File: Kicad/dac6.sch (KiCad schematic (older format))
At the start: 13 parts

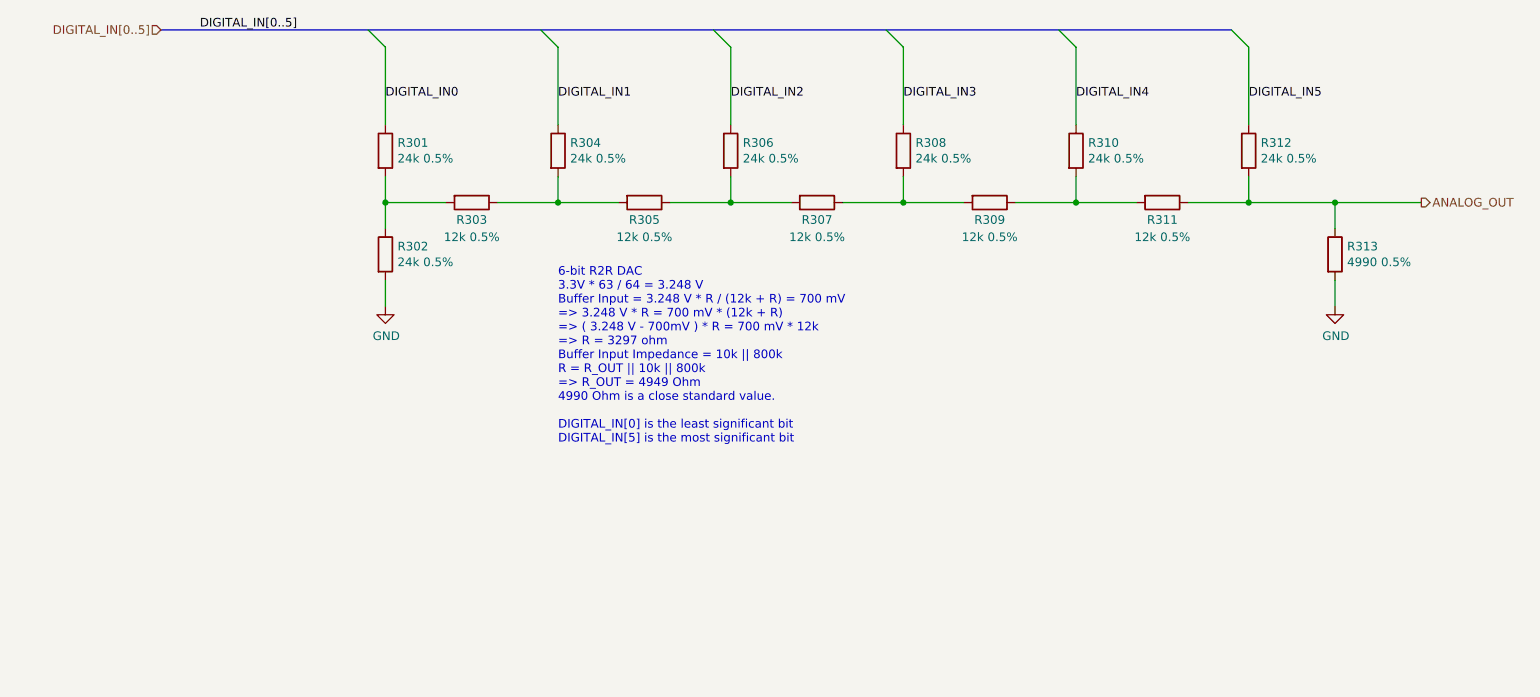
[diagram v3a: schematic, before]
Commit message: Changes to BMC
* Swapped BUTTON_PWR and SYS_RESET to avoid DRC issue
* Split PSU and BMC into two separate sheets
* Swapped some pins on the STM32 to make it compatible with more
alternatives
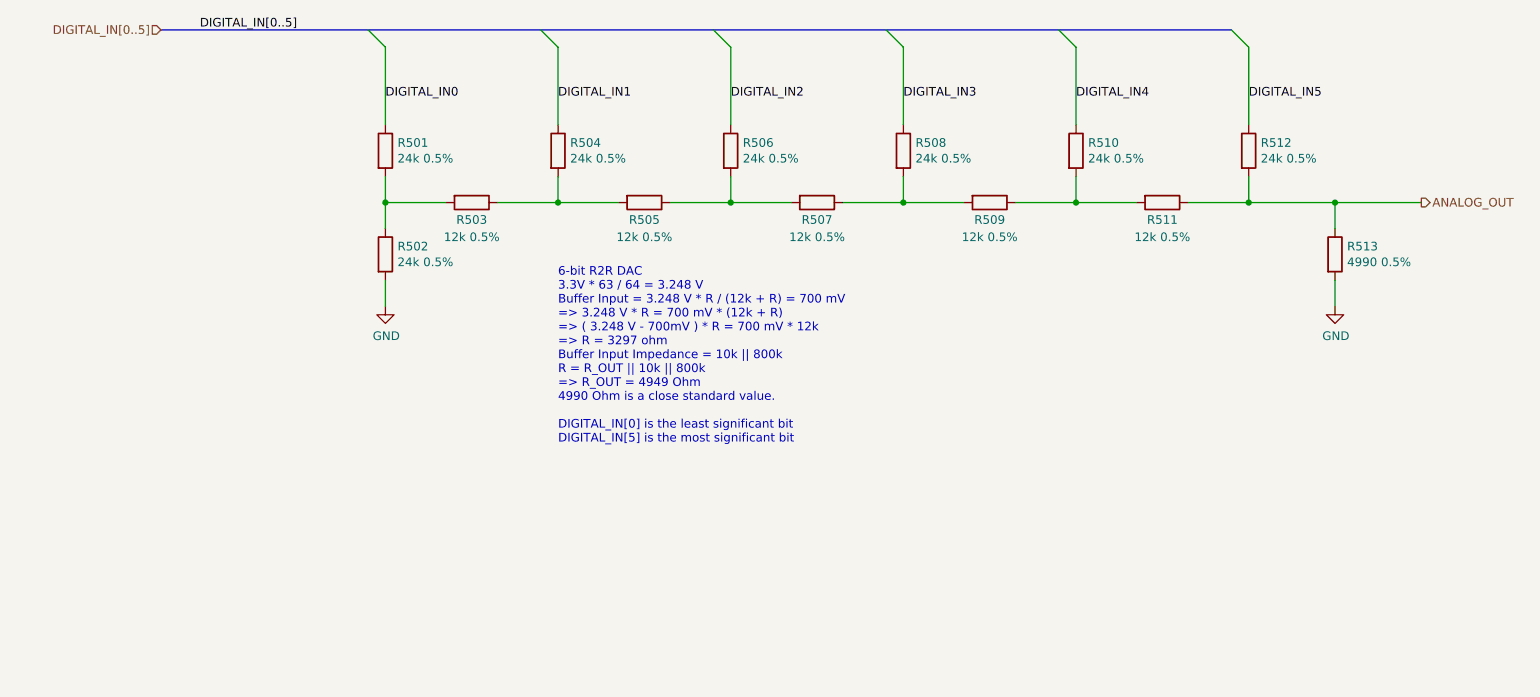
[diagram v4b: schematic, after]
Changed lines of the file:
@@
 $Descr A4 11693 8268
 encoding utf-8
-Sheet 3 16
+Sheet 3 17
 Title "Neotron Common Hardware - 6-bit DAC"
 Date "2021-04-02"
@@
 AR Path="/5FDE658D/60682025/60681FF8" Ref="R301"  Part="1"
 AR Path="/5FDE658D/6068202F/60681FF8" Ref="R501"  Part="1"
-F 0 "R301" H 3570 2746 50  0000 L CNN
+F 0 "R501" H 3570 2746 50  0000 L CNN
 F 1 "24k 0.5%" H 3570 2655 50  0000 L CNN
 F 2 "Resistor_SMD:R_0805_2012Metric_Pad1.20x1.40mm_HandSolder" V 3430 2700 50  0001 C CNN
@@
 AR Path="/5FDE658D/60682025/5F5F5C61" Ref="R303"  Part="1"
 AR Path="/5FDE658D/6068202F/5F5F5C61" Ref="R503"  Part="1"
-F 0 "R303" V 4100 3000 50  0000 C CNN
+F 0 "R503" V 4100 3000 50  0000 C CNN
 F 1 "12k 0.5%" V 4200 3000 50  0000 C CNN
 F 2 "Resistor_SMD:R_0805_2012Metric_Pad1.20x1.40mm_HandSolder" V 3930 3000 50  0001 C CNN
@@
 AR Path="/5FDE658D/60682025/5F5F6568" Ref="R304"  Part="1"
 AR Path="/5FDE658D/6068202F/5F5F6568" Ref="R504"  Part="1"
-F 0 "R304" H 4570 2746 50  0000 L CNN
+F 0 "R504" H 4570 2746 50  0000 L CNN
 F 1 "24k 0.5%" H 4570 2655 50  0000 L CNN
 F 2 "Resistor_SMD:R_0805_2012Metric_Pad1.20x1.40mm_HandSolder" V 4430 2700 50  0001 C CNN
@@
 AR Path="/5FDE658D/60682025/5F5F6D42" Ref="R305"  Part="1"
 AR Path="/5FDE658D/6068202F/5F5F6D42" Ref="R505"  Part="1"
-F 0 "R305" V 5100 3000 50  0000 C CNN
+F 0 "R505" V 5100 3000 50  0000 C CNN
 F 1 "12k 0.5%" V 5200 3000 50  0000 C CNN
 F 2 "Resistor_SMD:R_0805_2012Metric_Pad1.20x1.40mm_HandSolder" V 4930 3000 50  0001 C CNN
@@
 AR Path="/5FDE658D/60682025/5F5F6F45" Ref="R307"  Part="1"
 AR Path="/5FDE658D/6068202F/5F5F6F45" Ref="R507"  Part="1"
-F 0 "R307" V 6100 3000 50  0000 C CNN
+F 0 "R507" V 6100 3000 50  0000 C CNN
 F 1 "12k 0.5%" V 6200 3000 50  0000 C CNN
 F 2 "Resistor_SMD:R_0805_2012Metric_Pad1.20x1.40mm_HandSolder" V 5930 3000 50  0001 C CNN
@@
 AR Path="/5FDE658D/60682025/5F5F984D" Ref="R309"  Part="1"
 AR Path="/5FDE658D/6068202F/5F5F984D" Ref="R509"  Part="1"
-F 0 "R309" V 7100 3000 50  0000 C CNN
+F 0 "R509" V 7100 3000 50  0000 C CNN
 F 1 "12k 0.5%" V 7200 3000 50  0000 C CNN
 F 2 "Resistor_SMD:R_0805_2012Metric_Pad1.20x1.40mm_HandSolder" V 6930 3000 50  0001 C CNN
@@
 AR Path="/5FDE658D/60682025/5F5F99D6" Ref="R311"  Part="1"
 AR Path="/5FDE658D/6068202F/5F5F99D6" Ref="R511"  Part="1"
-F 0 "R311" V 8100 3000 50  0000 C CNN
+F 0 "R511" V 8100 3000 50  0000 C CNN
 F 1 "12k 0.5%" V 8200 3000 50  0000 C CNN
 F 2 "Resistor_SMD:R_0805_2012Metric_Pad1.20x1.40mm_HandSolder" V 7930 3000 50  0001 C CNN
@@
 AR Path="/5FDE658D/60682025/5F5FA2EE" Ref="R313"  Part="1"
 AR Path="/5FDE658D/6068202F/5F5FA2EE" Ref="R513"  Part="1"
-F 0 "R313" H 9070 3346 50  0000 L CNN
+F 0 "R513" H 9070 3346 50  0000 L CNN
 F 1 "4990 0.5%" H 9070 3255 50  0000 L CNN
 F 2 "Resistor_SMD:R_0805_2012Metric_Pad1.20x1.40mm_HandSolder" V 8930 3300 50  0001 C CNN
@@
 AR Path="/5FDE658D/60682025/5F5FBB89" Ref="#PWR0301"  Part="1"
 AR Path="/5FDE658D/6068202F/5F5FBB89" Ref="#PWR0501"  Part="1"
-F 0 "#PWR0301" H 3500 3350 50  0001 C CNN
+F 0 "#PWR0501" H 3500 3350 50  0001 C CNN
 F 1 "GND" H 3505 3427 50  0000 C CNN
 F 2 "" H 3500 3600 50  0001 C CNN
@@
 AR Path="/5FDE658D/60682025/5F5FBF42" Ref="#PWR0302"  Part="1"
 AR Path="/5FDE658D/6068202F/5F5FBF42" Ref="#PWR0502"  Part="1"
-F 0 "#PWR0302" H 9000 3350 50  0001 C CNN
+F 0 "#PWR0502" H 9000 3350 50  0001 C CNN
 F 1 "GND" H 9005 3427 50  0000 C CNN
 F 2 "" H 9000 3600 50  0001 C CNN
@@
 AR Path="/5FDE658D/60682025/5F5FCF8C" Ref="R302"  Part="1"
 AR Path="/5FDE658D/6068202F/5F5FCF8C" Ref="R502"  Part="1"
-F 0 "R302" H 3570 3346 50  0000 L CNN
+F 0 "R502" H 3570 3346 50  0000 L CNN
 F 1 "24k 0.5%" H 3570 3255 50  0000 L CNN
 F 2 "Resistor_SMD:R_0805_2012Metric_Pad1.20x1.40mm_HandSolder" V 3430 3300 50  0001 C CNN
@@
 AR Path="/5FDE658D/60682025/5F5FD13B" Ref="R306"  Part="1"
 AR Path="/5FDE658D/6068202F/5F5FD13B" Ref="R506"  Part="1"
-F 0 "R306" H 5570 2746 50  0000 L CNN
+F 0 "R506" H 5570 2746 50  0000 L CNN
 F 1 "24k 0.5%" H 5570 2655 50  0000 L CNN
 F 2 "Resistor_SMD:R_0805_2012Metric_Pad1.20x1.40mm_HandSolder" V 5430 2700 50  0001 C CNN
@@
 AR Path="/5FDE658D/60682025/60682004" Ref="R308"  Part="1"
 AR Path="/5FDE658D/6068202F/60682004" Ref="R508"  Part="1"
-F 0 "R308" H 6570 2746 50  0000 L CNN
+F 0 "R508" H 6570 2746 50  0000 L CNN
 F 1 "24k 0.5%" H 6570 2655 50  0000 L CNN
 F 2 "Resistor_SMD:R_0805_2012Metric_Pad1.20x1.40mm_HandSolder" V 6430 2700 50  0001 C CNN
@@
 AR Path="/5FDE658D/60682025/5F5FD46F" Ref="R310"  Part="1"
 AR Path="/5FDE658D/6068202F/5F5FD46F" Ref="R510"  Part="1"
-F 0 "R310" H 7570 2746 50  0000 L CNN
+F 0 "R510" H 7570 2746 50  0000 L CNN
 F 1 "24k 0.5%" H 7570 2655 50  0000 L CNN
 F 2 "Resistor_SMD:R_0805_2012Metric_Pad1.20x1.40mm_HandSolder" V 7430 2700 50  0001 C CNN
@@
 AR Path="/5FDE658D/60682025/5F5FD6C1" Ref="R312"  Part="1"
 AR Path="/5FDE658D/6068202F/5F5FD6C1" Ref="R512"  Part="1"
-F 0 "R312" H 8570 2746 50  0000 L CNN
+F 0 "R512" H 8570 2746 50  0000 L CNN
 F 1 "24k 0.5%" H 8570 2655 50  0000 L CNN
 F 2 "Resistor_SMD:R_0805_2012Metric_Pad1.20x1.40mm_HandSolder" V 8430 2700 50  0001 C CNN

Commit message: Brought in sheets from Neotron Pico.
Also includes DB15HD and PSU 3D models.
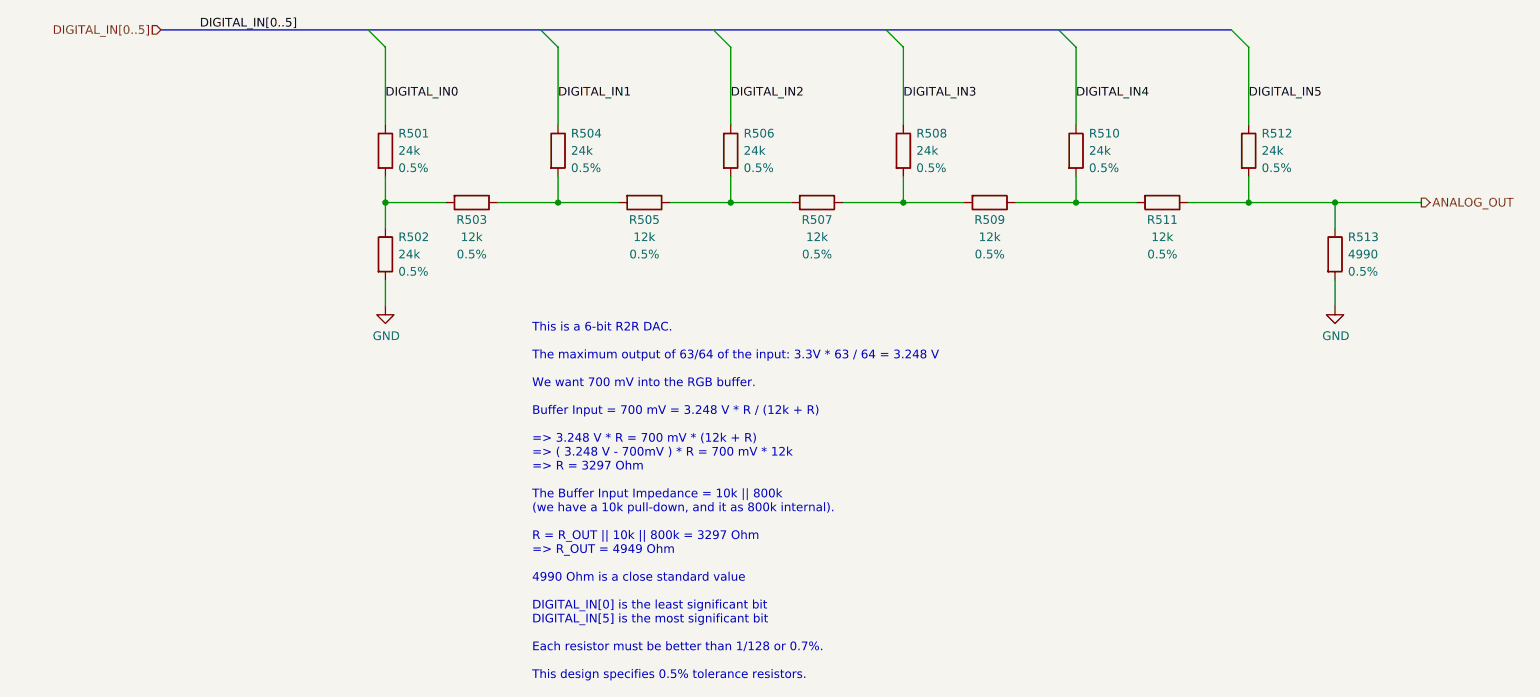
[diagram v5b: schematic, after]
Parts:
- R401, R402, R404, R406, R408, R410, R412: value 24k 0.5% -> 24k; Tolerance (none) -> 0.5%
- R403, R405, R407, R409, R411: value 12k 0.5% -> 12k; Tolerance (none) -> 0.5%
- R413: value 4990 0.5% -> 4990; Tolerance (none) -> 0.5%
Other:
- note added: "This is a 6-bit R2R DAC.\n\nThe maximum output of 63/64 of the input: 3.3V * 63 / 64 = 3.248 V\n\nWe want 700 mV into the RGB buffer.\n\nBuffer Input = 700 mV = 3.248 V * R / (12k + R)\n\n=> 3.248 V * R = 700 mV * (12k + R)\n=> ( 3.248 V - 700mV ) * R = 700 mV * 12k\n=> R = 3297 Ohm\n\nThe Buffer Input Impedance = 10k || 800k\n(we have a 10k pull-down, and it as 800k internal).\n\nR = R_OUT || 10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"
- note removed: "6-bit R2R DAC\n3.3V * 63 / 64 = 3.248 V\nBuffer Input = 3.248 V * R / (12k + R) = 700 mV\n=> 3.248 V * R = 700 mV * (12k + R)\n=> ( 3.248 V - 700mV ) * R = 700 mV * 12k\n=> R = 3297 ohm\nBuffer Input Impedance = 10k || 800k\nR = R_OUT || 10k || 800k\n=> R_OUT = 4949 Ohm\n4990 Ohm is a close standard value.\n\nDIGITAL_IN[0] is the least significant bit\nDIGITAL_IN[5] is the most significant bit\n"
